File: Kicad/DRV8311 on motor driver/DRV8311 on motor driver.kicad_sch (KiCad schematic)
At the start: 20 parts, among them J3 1mm pitch board edge, U2 DRV8311HRRWR

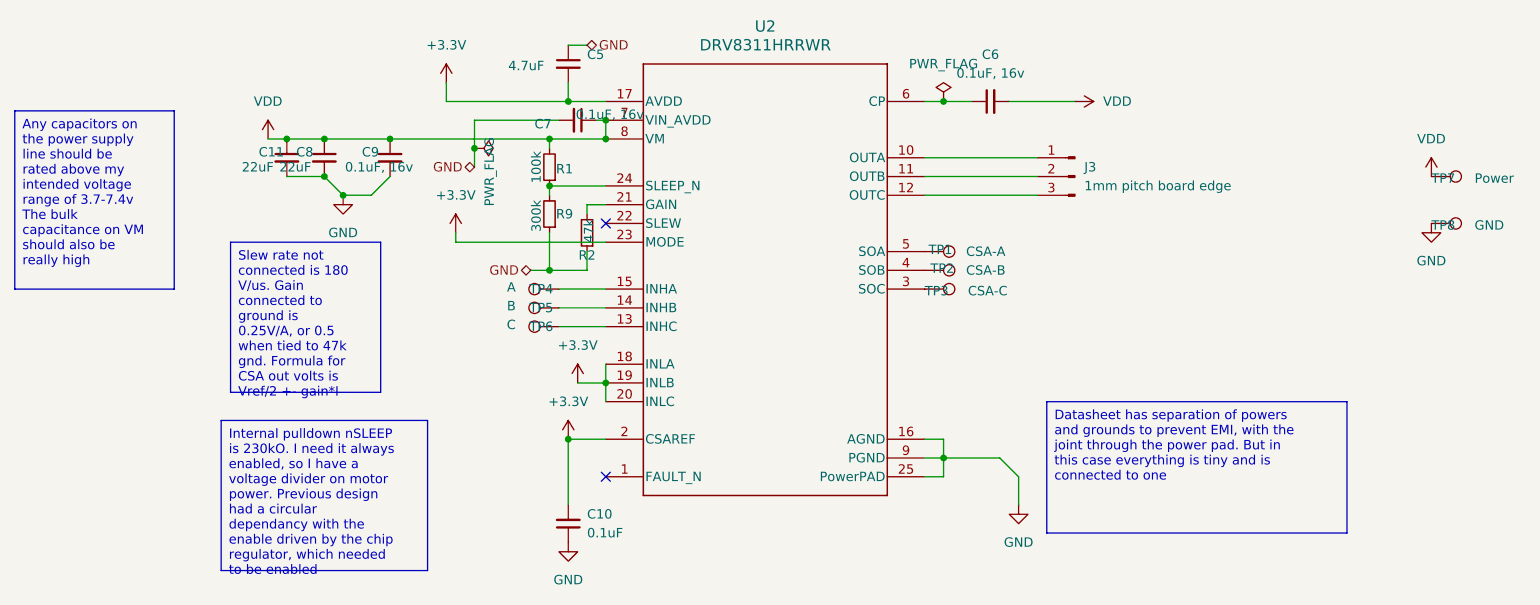
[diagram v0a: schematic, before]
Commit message: Fixed kicad schematic errors, arranged pads
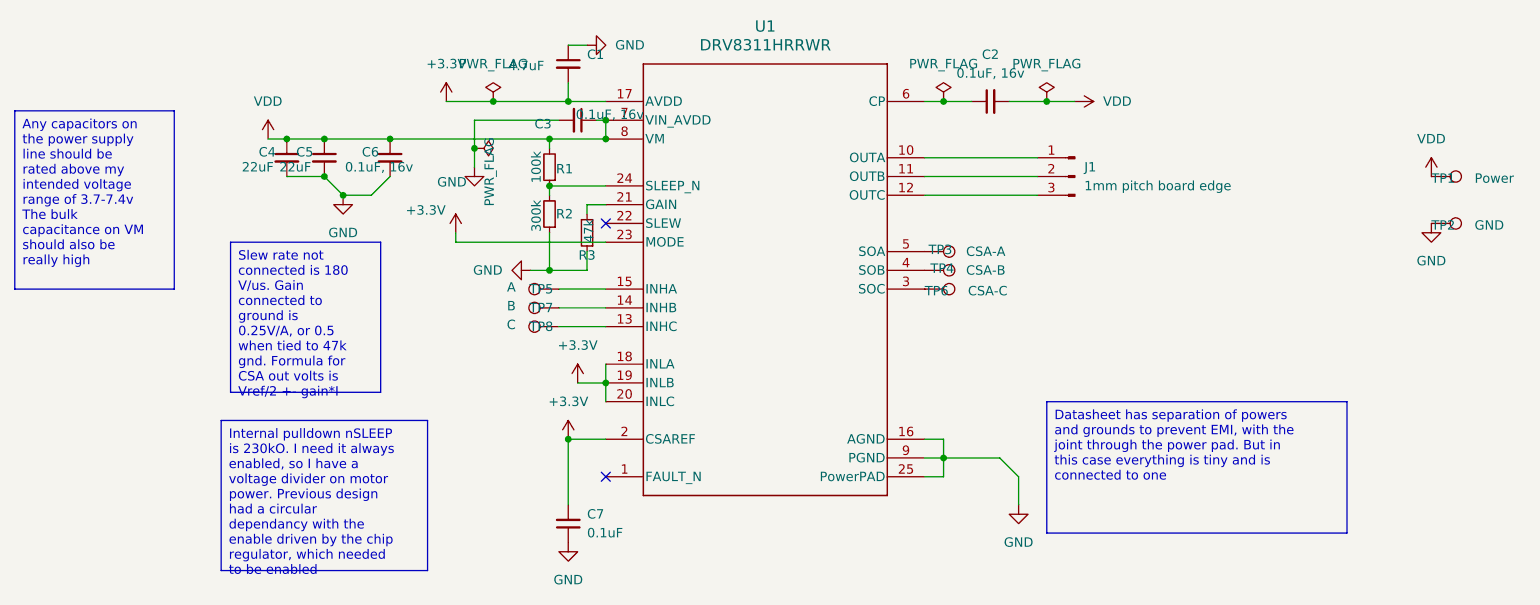
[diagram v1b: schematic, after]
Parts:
- renumbered C5 to C1, C6 to C2, C7 to C3, C11 to C4, C8 to C5, C9 to C6, C10 to C7, J3 to J1, R9 to R2, R2 to R3, TP7 to TP1, TP8 to TP2, TP1 to TP3, TP2 to TP4, TP4 to TP5, TP3 to TP6, TP5 to TP7, TP6 to TP8, U2 to U1

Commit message: Finished component layout
The current board diameter is 12mm, though I may be able to shrink it down to 10mm. Its already REALLY small, with those 0402 components. It would be nice if the board didn't exceed the outer diameter of the motor.
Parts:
- J1: footprint Connector_PinHeader_1.00mm:PinHeader_1x03_P1.00mm_Vertical -> Connector_PinHeader_1.27mm:PinHeader_1x03_P1.27mm_Vertical
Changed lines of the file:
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@@
 			)
 		)
-		(property "Footprint" "Connector_PinHeader_1.00mm:PinHeader_1x03_P1.00mm_Vertical"
+		(property "Footprint" "Connector_PinHeader_1.27mm:PinHeader_1x03_P1.27mm_Vertical"
 			(at 171.45 64.77 0)
 			(effects

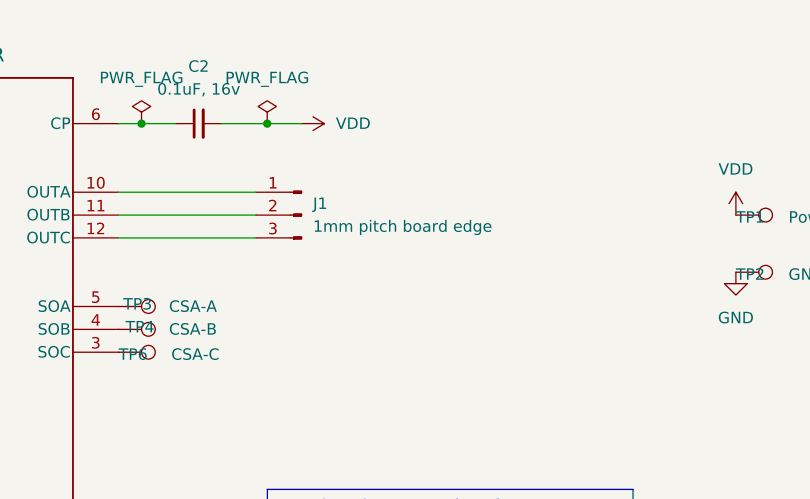
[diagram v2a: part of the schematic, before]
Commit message: Finished routing, distribute pwr planes, silkscreen and DRC check
The power planes were not making good connection previously, so I have fixed that.
Silkscreen is done, the last traces have been routed, and there isn't much I can do
As far as I'm concerned, this board is done!
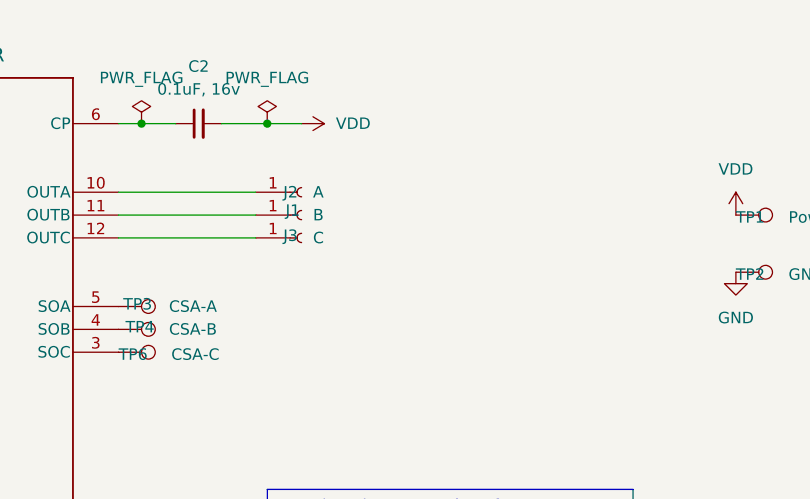
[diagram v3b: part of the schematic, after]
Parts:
- removed J1: 1mm pitch board edge, Connector_PinHeader_1.27mm:PinHeader_1x03_P1.27mm_Vertical, symbol Connector:Conn_01x03_Pin
- added J1: B, custom_testpoints:PinHeader_1x01_P1.27mm_Round, symbol Connector:Conn_01x01_Socket
- added J2: A, custom_testpoints:PinHeader_1x01_P1.27mm_Round, symbol Connector:Conn_01x01_Socket
- added J3: C, custom_testpoints:PinHeader_1x01_P1.27mm_Round, symbol Connector:Conn_01x01_Socket
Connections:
- net at U1.10 (OUTA): now also J2.1 (Pin_1)
- net at U1.11 (OUTB): now also J1.1 (Pin_1)
- net at U1.12 (OUTC): now also J3.1 (Pin_1)
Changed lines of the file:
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@@
+	)
+	(symbol
+		(lib_id "Connector:Conn_01x01_Socket")
+		(at 171.45 62.23 0)
+		(unit 1)
+		(exclude_from_sim no)
+		(in_bom yes)
+		(on_board yes)
+		(dnp no)
+		(property "Reference" "J2"
+			(at 169.418 62.23 0)
+			(effects
+				(font
+					(size 1.27 1.27)
+				)
+				(justify left)
+			)
+		)
+		(property "Value" "A"
+			(at 172.72 62.23 0)
+			(effects
+				(font
+					(size 1.27 1.27)
+				)
+				(justify left)
+			)
+		)
+		(property "Footprint" "custom_testpoints:PinHeader_1x01_P1.27mm_Round"
+			(at 171.45 62.23 0)
+			(effects
+				(font
+					(size 1.27 1.27)
+				)
+				(hide yes)
+			)
+		)
+		(property "Datasheet" "~"
+			(at 171.45 62.23 0)
+			(effects
+				(font
+					(size 1.27 1.27)
+				)
+				(hide yes)
+			)
+		)
+		(property "Description" "Generic connector, single row, 01x01, script generated"
+			(at 171.45 62.23 0)
+			(effects
+				(font
+					(size 1.27 1.27)
+				)
+				(hide yes)
+			)
+		)
+		(pin "1"
+		)
+		(instances
+			(project ""
+				(path "/8760dbe3-976e-4366-afd9-aec15b99495c"
+					(reference "J2")
+					(unit 1)
+				)
+			)
+		)
+	)
+	(symbol
+		(lib_id "Connector:Conn_01x01_Socket")
+		(at 171.45 64.77 0)
+		(unit 1)
+		(exclude_from_sim no)
+		(in_bom yes)
+		(on_board yes)
+		(dnp no)
+		(property "Reference" "J1"
+			(at 169.672 64.262 0)
+			(effects
+				(font
+					(size 1.27 1.27)
+				)
+				(justify left)
+			)
+		)
+		(property "Value" "B"
+			(at 172.72 64.77 0)
+			(effects
+				(font
+					(size 1.27 1.27)
+				)
+				(justify left)
+			)
+		)
+		(property "Footprint" "custom_testpoints:PinHeader_1x01_P1.27mm_Round"
+			(at 171.45 64.77 0)
+			(effects
+				(font
+					(size 1.27 1.27)
+				)
+				(hide yes)
+			)
+		)
+		(property "Datasheet" "~"
+			(at 171.45 64.77 0)
+			(effects
+				(font
+					(size 1.27 1.27)
+				)
+				(hide yes)
+			)
+		)
+		(property "Description" "Generic connector, single row, 01x01, script generated"
+			(at 171.45 64.77 0)
+			(effects
+				(font
+					(size 1.27 1.27)
+				)
+				(hide yes)
+			)
+		)
+		(pin "1"
+		)
+		(instances
+			(project "DRV8311 on motor driver"
+				(path "/8760dbe3-976e-4366-afd9-aec15b99495c"
+					(reference "J1")
+					(unit 1)
+				)
+			)
+		)
 	)
 	(symbol
@@
 	)
 	(symbol
-		(lib_id "Connector:Conn_01x03_Pin")
-		(at 171.45 64.77 180)
-		(unit 1)
-		(exclude_from_sim no)
-		(in_bom yes)
-		(on_board yes)
-		(dnp no)
-		(fields_autoplaced yes)
-		(property "Reference" "J1"
-			(at 172.72 63.4999 0)
-			(effects
-				(font
-					(size 1.27 1.27)
-				)
-				(justify right)
-			)
-		)
-		(property "Value" "1mm pitch board edge"
-			(at 172.72 66.0399 0)
-			(effects
-				(font
-					(size 1.27 1.27)
-				)
-				(justify right)
-			)
-		)
-		(property "Footprint" "Connector_PinHeader_1.27mm:PinHeader_1x03_P1.27mm_Vertical"
-			(at 171.45 64.77 0)
-			(effects
-				(font
-					(size 1.27 1.27)
-				)
-				(hide yes)
-			)
-		)
-		(property "Datasheet" "~"
-			(at 171.45 64.77 0)
-			(effects
-				(font
-					(size 1.27 1.27)
-				)
-				(hide yes)
-			)
-		)
-		(property "Description" "Generic connector, single row, 01x03, script generated"
-			(at 171.45 64.77 0)
-			(effects
-				(font
-					(size 1.27 1.27)
-				)
-				(hide yes)
-			)
-		)
-		(pin "3"
-		)
-		(pin "1"
-		)
-		(pin "2"
-		)
-		(instances
-			(project ""
-				(path "/8760dbe3-976e-4366-afd9-aec15b99495c"
-					(reference "J1")
-					(unit 1)
-				)
-			)
-			(project "stm32g070 and DRV8311 single motor board - V1 Alpha"
-				(path "/eb3f183d-8bb1-43a5-a363-092ed67891e3/5c02fed6-da20-4eef-a2eb-99e8043b232c"
-					(reference "J3")
-					(unit 1)
-				)
-			)
-		)
-	)
-	(symbol
 		(lib_id "power:+3.3V")
 		(at 86.36 54.61 0)
@@
 					(unit 1)
 				)
+			)
+		)
+	)
+	(symbol
+		(lib_id "Connector:Conn_01x01_Socket")
+		(at 171.45 67.31 0)
+		(unit 1)
+		(exclude_from_sim no)
+		(in_bom yes)
+		(on_board yes)
+		(dnp no)
+		(property "Reference" "J3"
+			(at 169.418 67.056 0)
+			(effects
+				(font
+					(size 1.27 1.27)
+				)
+				(justify left)
+			)
+		)
+		(property "Value" "C"
+			(at 172.72 67.31 0)
+			(effects
+				(font
+					(size 1.27 1.27)
+				)
+				(justify left)
+			)
+		)
+		(property "Footprint" "custom_testpoints:PinHeader_1x01_P1.27mm_Round"
+			(at 171.45 67.31 0)
+			(effects
+				(font
+					(size 1.27 1.27)
+				)
+				(hide yes)
+			)
+		)
+		(property "Datasheet" "~"
+			(at 171.45 67.31 0)
+			(effects
+				(font
+					(size 1.27 1.27)
+				)
+				(hide yes)
+			)
+		)
+		(property "Description" "Generic connector, single row, 01x01, script generated"
+			(at 171.45 67.31 0)
+			(effects
+				(font
+					(size 1.27 1.27)
+				)
+				(hide yes)
+			)
+		)
+		(pin "1"
+		)
+		(instances
+			(project "DRV8311 on motor driver"
+				(path "/8760dbe3-976e-4366-afd9-aec15b99495c"
+					(reference "J3")
+					(unit 1)
+				)

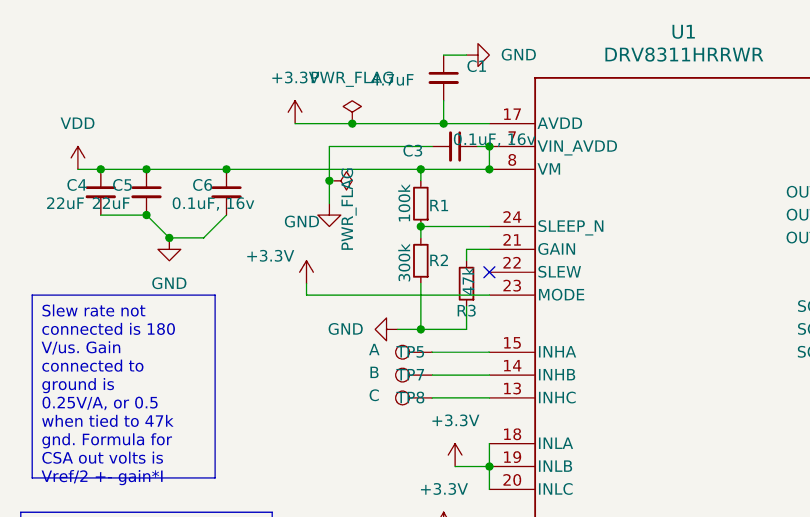
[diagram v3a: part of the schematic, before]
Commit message: Fixed small issue on Driver board resistor values swapped
I switched it from 100k over 300k, to 300k over 100k. If the input is 8.4 volts, the output should be 2.1 volts. Small mistake.
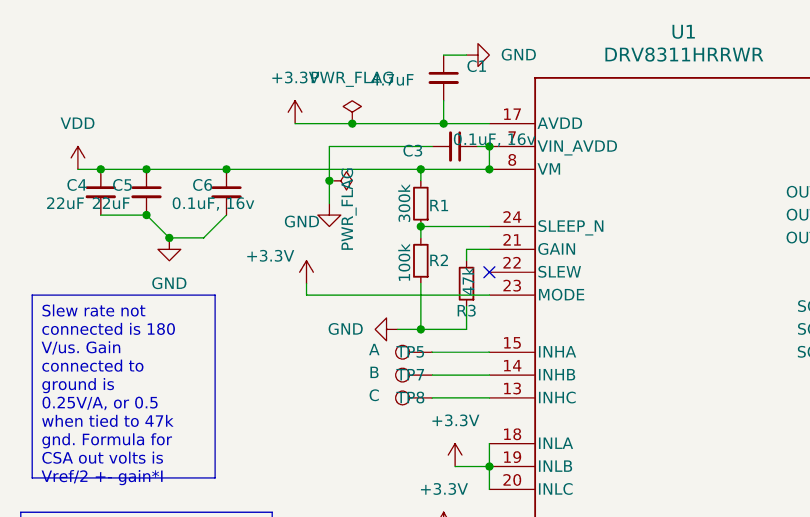
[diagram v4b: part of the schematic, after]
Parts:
- R1: value 100k -> 300k
- R2: value 300k -> 100k
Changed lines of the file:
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@@
 			)
 		)
-		(property "Value" "100k"
+		(property "Value" "300k"
 			(at 98.552 63.5 90)
 			(effects
@@
 			)
 		)
-		(property "Value" "300k"
+		(property "Value" "100k"
 			(at 98.552 70.104 90)
 			(effects

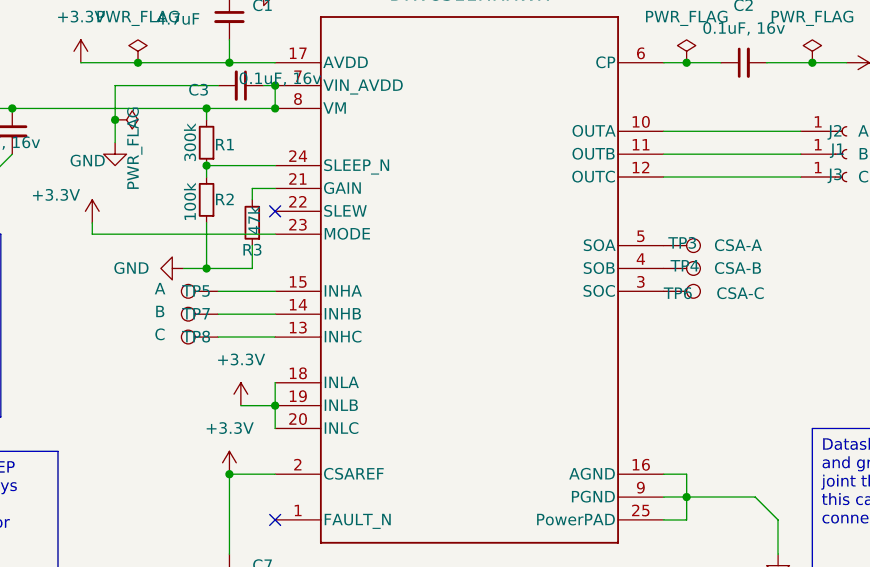
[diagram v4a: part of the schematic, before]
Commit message: Gerbers and BOM for v0.4 PCB
I adjusted all the testpoints to be excluded from the BOM.
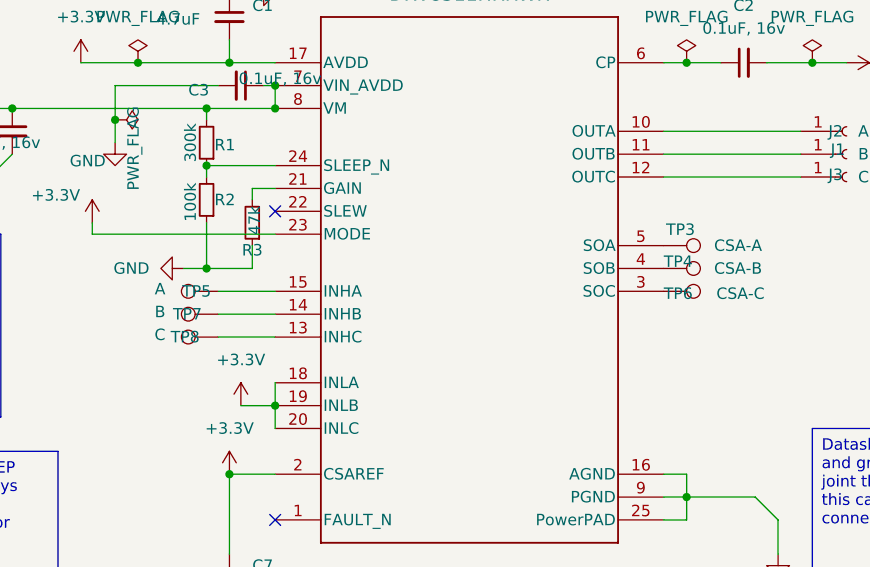
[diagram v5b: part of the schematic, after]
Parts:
- J1, J2, J3, TP1, TP2, TP3, TP4, TP5, TP6, TP7, TP8: now left out of the parts list
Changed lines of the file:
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@@
 		(unit 1)
 		(exclude_from_sim no)
-		(in_bom yes)
+		(in_bom no)
 		(on_board yes)
 		(dnp no)
@@
 		(unit 1)
 		(exclude_from_sim no)
-		(in_bom yes)
+		(in_bom no)
 		(on_board yes)
 		(dnp no)
@@
 		(unit 1)
 		(exclude_from_sim no)
-		(in_bom yes)
+		(in_bom no)
 		(on_board yes)
 		(dnp no)
@@
 		(unit 1)
 		(exclude_from_sim no)
-		(in_bom yes)
+		(in_bom no)
 		(on_board yes)
 		(dnp no)
 		(property "Reference" "TP8"
-			(at 100.838 85.09 90)
+			(at 99.568 85.09 90)
 			(effects
 				(font
@@
 		(unit 1)
 		(exclude_from_sim no)
-		(in_bom yes)
+		(in_bom no)
 		(on_board yes)
 		(dnp no)
 		(property "Reference" "TP7"
-			(at 100.838 82.55 90)
+			(at 99.822 82.55 90)
 			(effects
 				(font
@@
 		(unit 1)
 		(exclude_from_sim no)
-		(in_bom yes)
+		(in_bom no)
 		(on_board yes)
 		(dnp no)
 		(property "Reference" "TP3"
-			(at 151.638 74.676 90)
+			(at 151.384 73.152 90)
 			(effects
 				(font
@@
 		(unit 1)
 		(exclude_from_sim no)
-		(in_bom yes)
+		(in_bom no)
 		(on_board yes)
 		(dnp no)
@@
 		(unit 1)
 		(exclude_from_sim no)
-		(in_bom yes)
+		(in_bom no)
 		(on_board yes)
 		(dnp no)
 		(property "Reference" "TP4"
-			(at 151.892 77.216 90)
+			(at 151.13 76.708 90)
 			(effects
 				(font
@@
 		(unit 1)
 		(exclude_from_sim no)
-		(in_bom yes)
+		(in_bom no)
 		(on_board yes)
 		(dnp no)
@@
 		(unit 1)
 		(exclude_from_sim no)
-		(in_bom yes)
+		(in_bom no)
 		(on_board yes)
 		(dnp no)
@@
 		(unit 1)
 		(exclude_from_sim no)
-		(in_bom yes)
-		(on_board yes)
-		(dnp no)
+		(in_bom no)
+		(on_board yes)
+		(dnp no)
